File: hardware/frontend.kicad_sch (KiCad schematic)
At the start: 92 parts, among them IC201 FMMT458TA, J201 Conn_01x02, J202 Conn_01x02, J203 Conn_01x02, J204 Conn_01x02, J205 Conn_01x02, Q201 2N7002, U201 BQ769x2

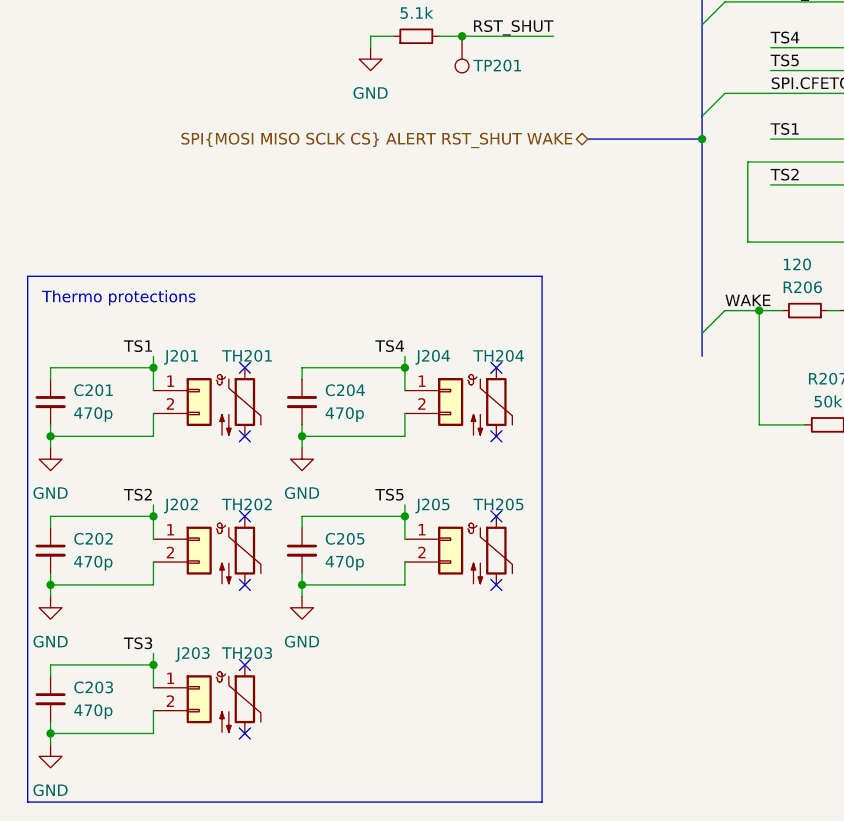
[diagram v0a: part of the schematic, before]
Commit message: change add thermoprotection
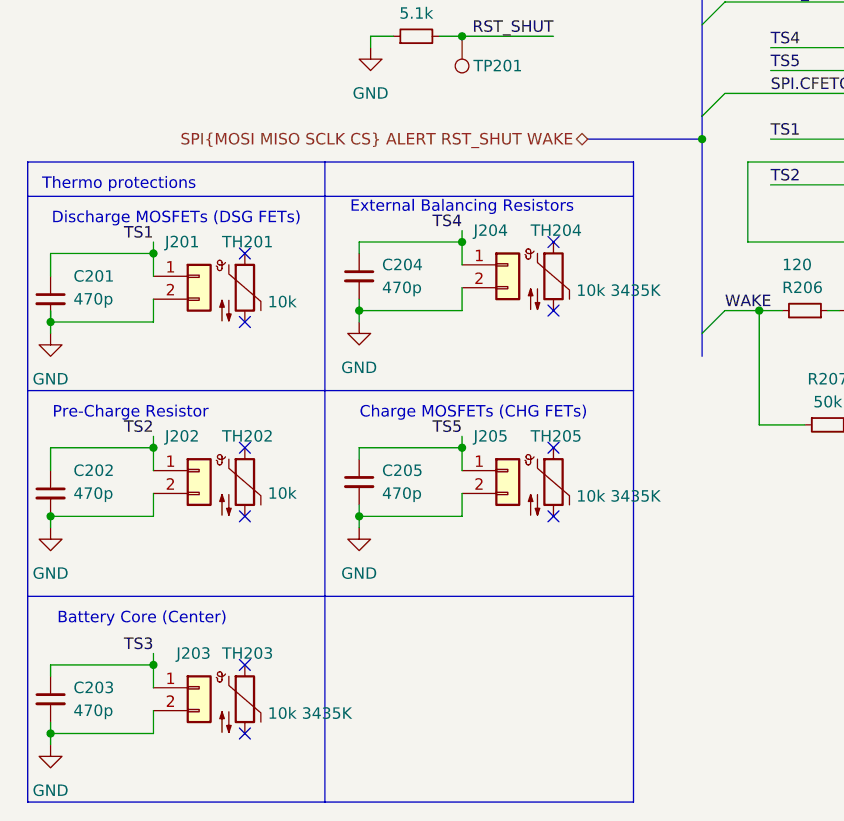
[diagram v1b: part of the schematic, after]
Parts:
- TH201, TH202: value Thermistor_NTC -> 10k; LCSC (none) -> C84036
- TH203, TH204, TH205: value Thermistor_NTC -> 10k 3435K; LCSC (none) -> C84036
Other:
- note added: "Battery Core (Center)"
- note added: "Charge MOSFETs (CHG FETs)"
- note added: "Discharge MOSFETs (DSG FETs)"
- note added: "External Balancing Resistors"
- note added: "Pre-Charge Resistor"
- moved on the sheet: C201, C202, C204, C205, J201, J202, J204, J205, TH201, TH202, TH204, TH205

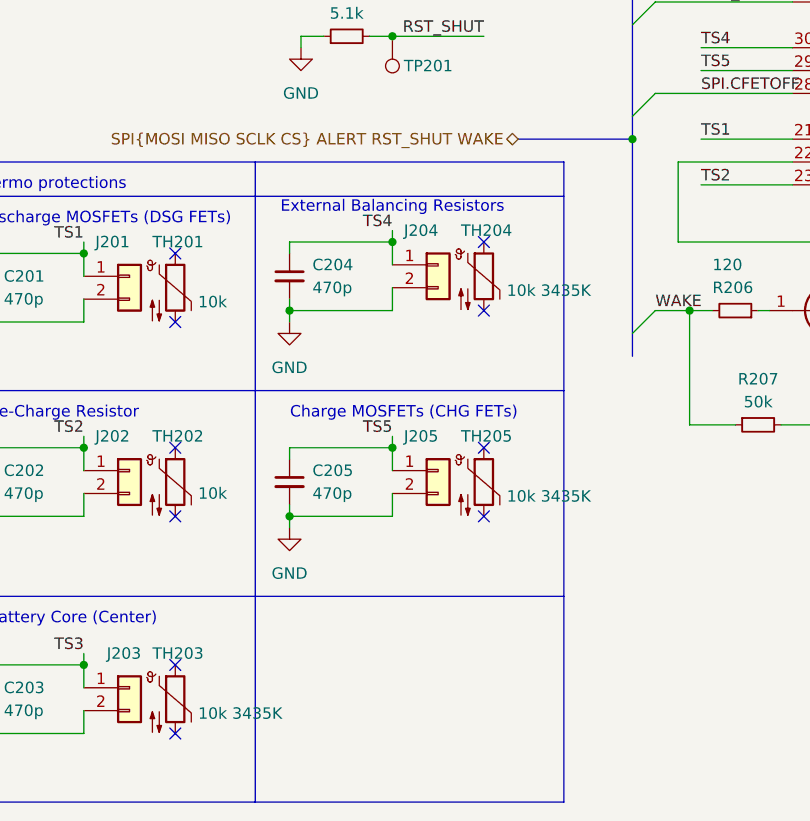
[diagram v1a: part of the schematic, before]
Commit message: change add thermoprotection
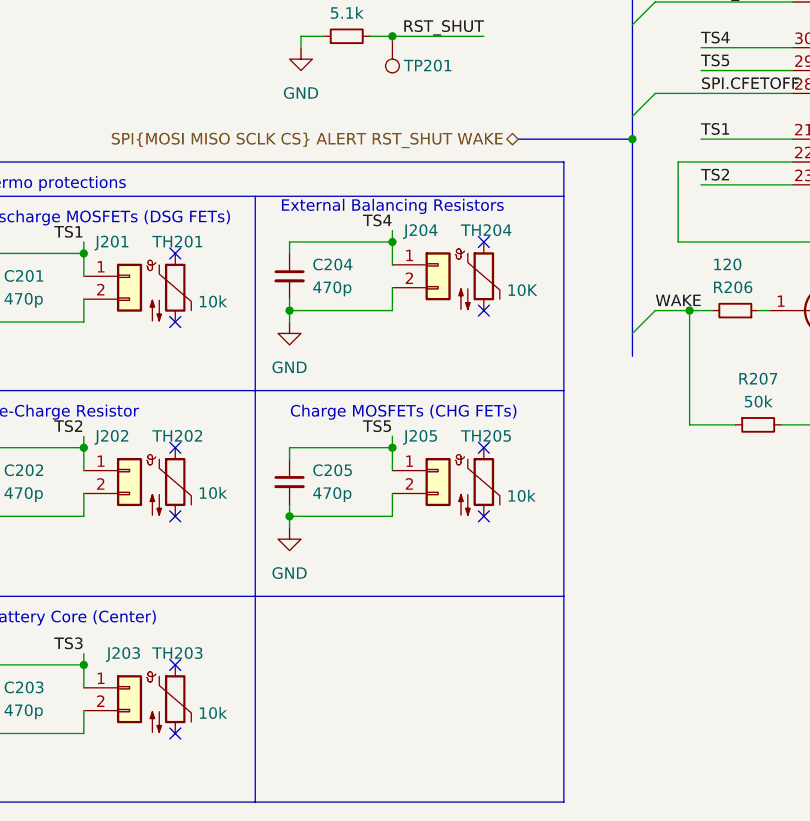
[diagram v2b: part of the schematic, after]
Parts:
- TH203, TH205: value 10k 3435K -> 10k
- TH204: value 10k 3435K -> 10K
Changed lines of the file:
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@@
 	(polyline
 		(pts
-			(xy 46.99 125.73) (xy 46.99 196.85)
+			(xy 46.99 129.54) (xy 46.99 196.85)
 		)
 		(stroke
@@
 			)
 		)
-		(property "Value" "10k 3435K"
+		(property "Value" "10K"
 			(at 74.93 140.0174 0)
 			(show_name no)
@@
 			)
 		)
-		(property "Value" "10k 3435K"
+		(property "Value" "10k"
 			(at 40.64 187.0074 0)
 			(show_name no)
@@
 			)
 		)
-		(property "Value" "10k 3435K"
+		(property "Value" "10k"
 			(at 74.93 162.8774 0)
 			(show_name no)

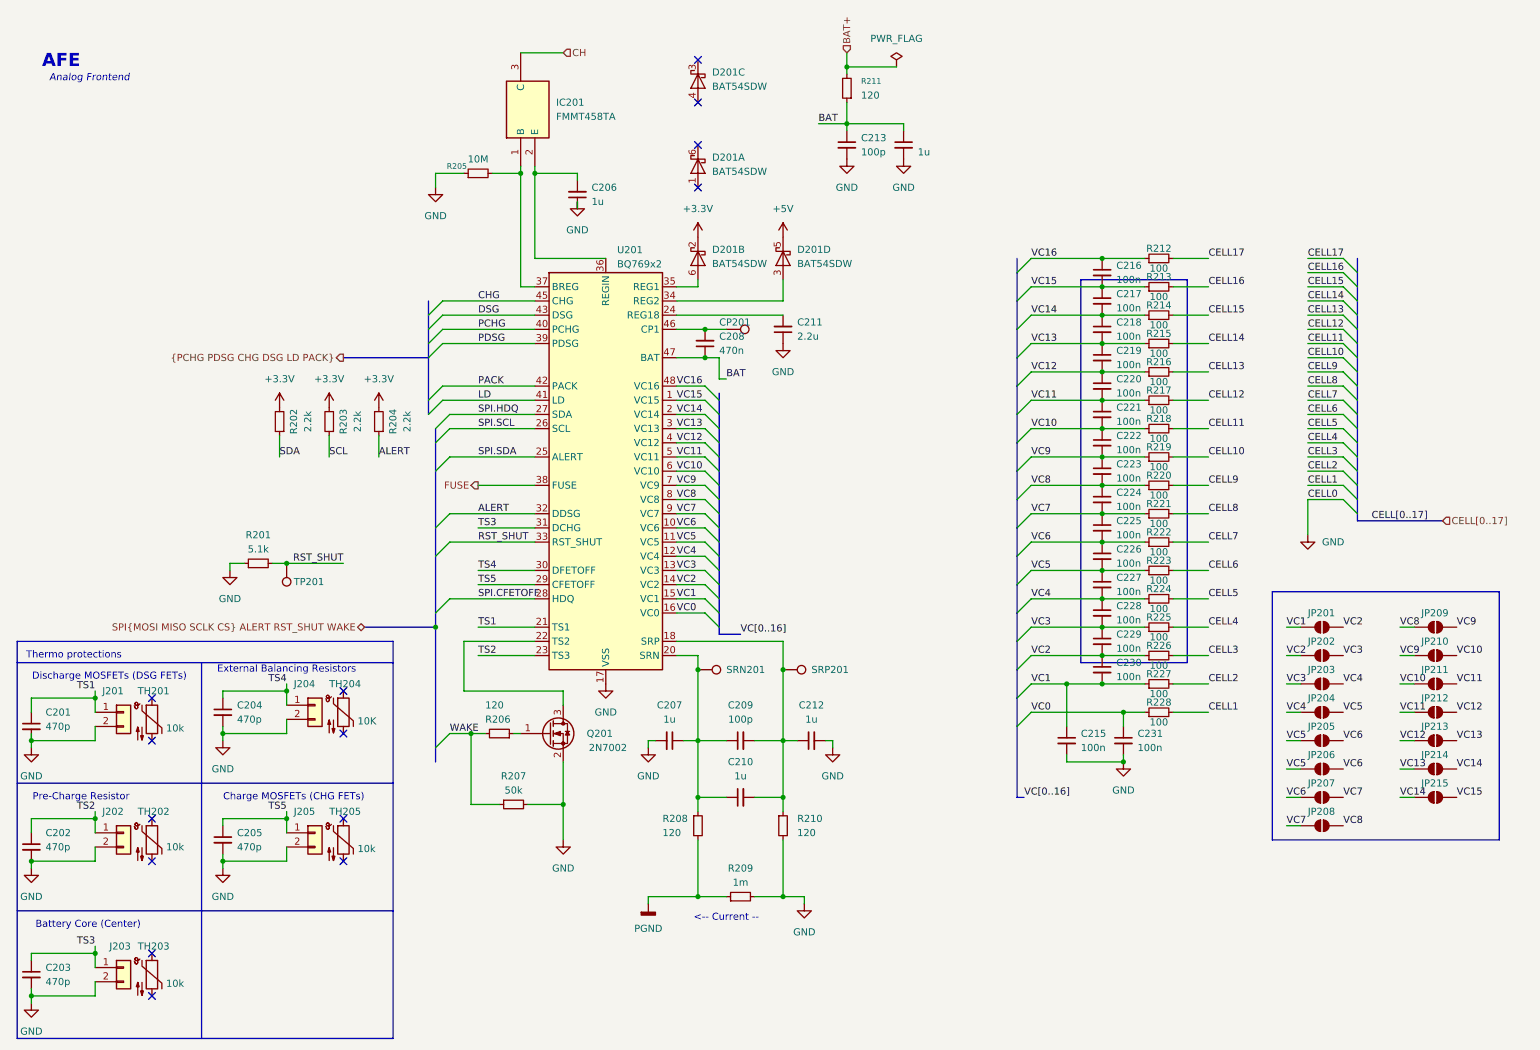
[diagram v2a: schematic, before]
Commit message: change change n transistor symbol
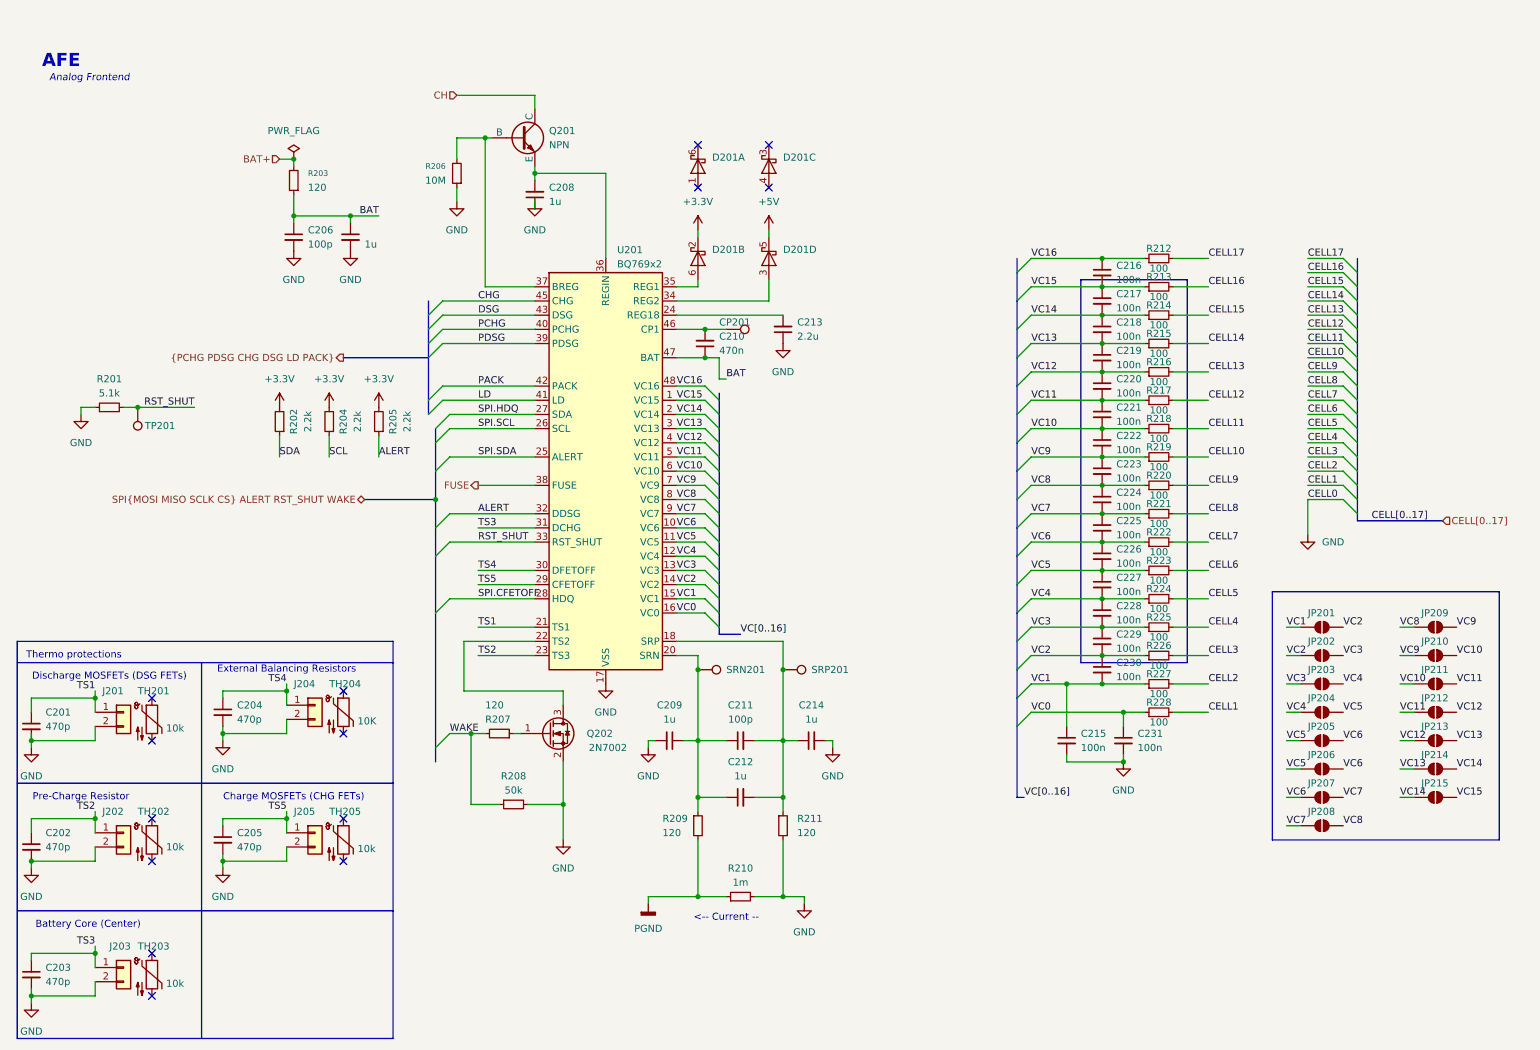
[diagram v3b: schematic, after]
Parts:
- removed IC201: FMMT458TA, Samacsys:SOT96P240X110-3N, symbol Samacsys:FMMT458TA
- added Q201: NPN, Samacsys:SOT96P240X110-3N, symbol Simulation_SPICE:NPN
- renumbered C213 to C206, C214 to C207, C206 to C208, C207 to C209, C208 to C210, C209 to C211, C210 to C212, C211 to C213, C212 to C214, Q201 to Q202, R211 to R203, R203 to R204, R204 to R205, R205 to R206, R206 to R207, R207 to R208, R208 to R209, R209 to R210, R210 to R211
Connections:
- net CH: now also Q201.1 (C)
- net at R206.2, U201.37 (BREG): now also Q201.2 (B)
- net at C208.2, U201.36 (REGIN): now also Q201.3 (E)
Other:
- moved on the sheet: C206, C208, D201C, D201D, R201, R203, R206, TP201

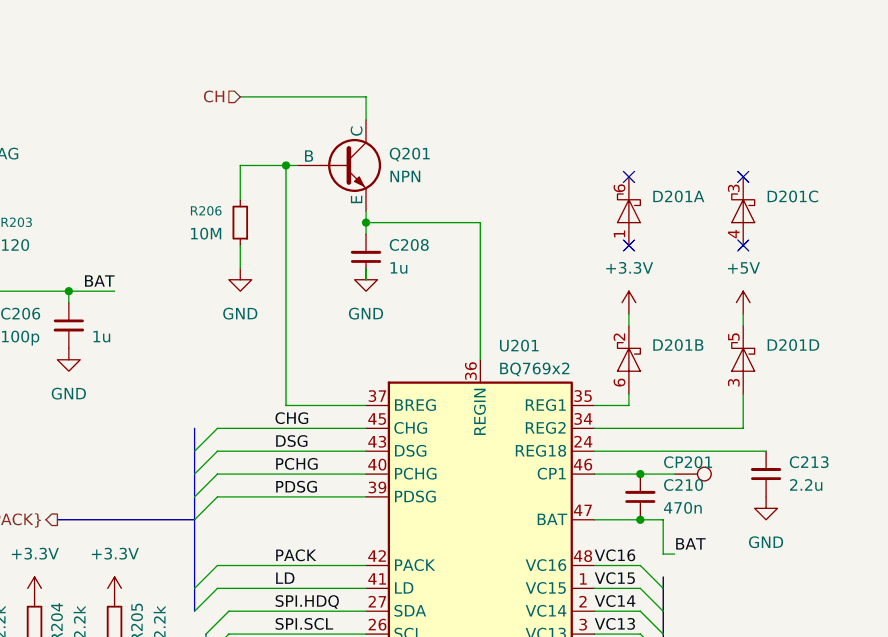
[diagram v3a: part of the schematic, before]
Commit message: hide symbols
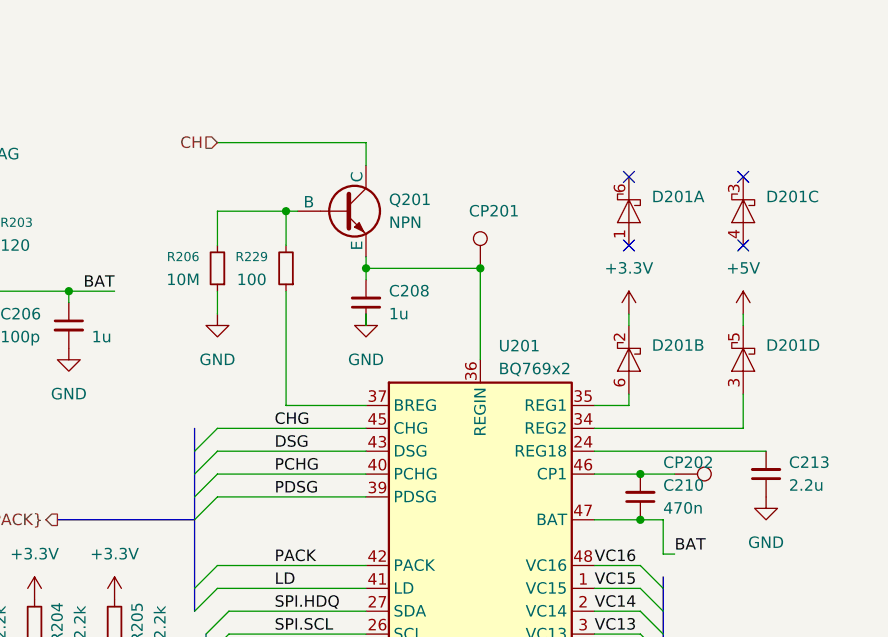
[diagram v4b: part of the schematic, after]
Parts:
- added CP201: TestPoint, TestPoint:TestPoint_Pad_D1.0mm, symbol Connector:TestPoint
- added R229: 100, Resistor_SMD:R_0805_2012Metric, symbol Device:R_Small
- renumbered CP201 to CP202
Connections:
- net at Q201.2 (B), R206.2: now also R229.2; no longer U201.37 (BREG)
- net at C208.2, Q201.3 (E), U201.36 (REGIN): now also CP201.1
- new net: R229.1, U201.37 (BREG)
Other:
- moved on the sheet: C208, Q201, R206

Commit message: fix SPI pins
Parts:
- added D202: SS110, Diode_SMD:D_SMA, symbol Device:D
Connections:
- net SPI.SDA is gone; now on net ALERT: U201.25 (ALERT)
- net ALERT: no longer U201.32 (DDSG)
- net CELL17: now also D202.2 (A)
- net TS5: now also U201.32 (DDSG); no longer U201.29 (CFETOFF)
- net CH: no longer names the net of Q201.1 (C)
- net CH: now also D202.1 (K)
- net SPI.CFETOFF renamed SPI.MOSI
- net SPI.HDQ renamed SPI.MISO
- net SPI.SCL renamed SPI.SCLK
- new net SPI.CS: U201.29 (CFETOFF)
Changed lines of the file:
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@@
 	)
 	(bus_entry
+		(at 88.9 118.11)
+		(size 2.54 -2.54)
+		(stroke
+			(width 0)
+			(type default)
+		)
+	)
+	(bus_entry
 		(at 91.44 142.24)
 		(size -2.54 2.54)
@@
 	)
 	(bus_entry
-		(at 88.9 105.41)
-		(size 2.54 -2.54)
-		(stroke
-			(width 0)
-			(type default)
-		)
-	)
-	(bus_entry
 		(at 251.46 77.47)
 		(size 2.54 2.54)
@@
 	(wire
 		(pts
-			(xy 91.44 102.87) (xy 106.68 102.87)
-		)
-		(stroke
-			(width 0)
-			(type default)
-		)
-	)
-	(wire
-		(pts
 			(xy 220.98 77.47) (xy 227.33 77.47)
 		)
@@
 	(wire
 		(pts
+			(xy 90.17 33.02) (xy 96.52 33.02)
+		)
+		(stroke
+			(width 0)
+			(type default)
+		)
+	)
+	(wire
+		(pts
 			(xy 261.62 153.67) (xy 264.16 153.67)
 		)
@@
 	(wire
 		(pts
+			(xy 91.44 115.57) (xy 106.68 115.57)
+		)
+		(stroke
+			(width 0)
+			(type default)
+		)
+	)
+	(wire
+		(pts
 			(xy 151.13 153.67) (xy 151.13 156.21)
 		)
@@
 	(wire
 		(pts
+			(xy 96.52 102.87) (xy 106.68 102.87)
+		)
+		(stroke
+			(width 0)
+			(type default)
+		)
+	)
+	(wire
+		(pts
 			(xy 111.76 147.32) (xy 111.76 154.94)
 		)
@@
 		)
 	)
-	(wire
-		(pts
-			(xy 96.52 115.57) (xy 106.68 115.57)
-		)
-		(stroke
-			(width 0)
-			(type default)
-		)
-	)
 	(bus
 		(pts
@@
 	(wire
 		(pts
+			(xy 104.14 33.02) (xy 106.68 33.02)
+		)
+		(stroke
+			(width 0)
+			(type default)
+		)
+	)
+	(wire
+		(pts
 			(xy 132.08 95.25) (xy 137.16 95.25)
 		)
@@
 	(wire
 		(pts
-			(xy 106.68 33.02) (xy 90.17 33.02)
-		)
-		(stroke
-			(width 0)
-			(type default)
-		)
-	)
-	(wire
-		(pts
 			(xy 195.58 77.47) (xy 208.28 77.47)
 		)
@@
 		)
 	)
-	(label "SPI.HDQ"
+	(label "SPI.MISO"
 		(at 96.52 85.09 0)
 		(effects
@@
 		)
 	)
-	(label "TS5"
-		(at 96.52 115.57 0)
-		(effects
-			(font
-				(size 1.27 1.27)
-			)
-			(justify left bottom)
-		)
-	)
-	(label "SPI.CFETOFF"
+	(label "SPI.MOSI"
 		(at 96.52 118.11 0)
 		(effects
@@
 		)
 	)
-	(label "SPI.SDA"
-		(at 96.52 92.71 0)
-		(effects
-			(font
-				(size 1.27 1.27)
-			)
-			(justify left bottom)
-		)
-	)
 	(label "VC6"
 		(at 251.46 148.59 0)
@@
 		)
 	)
+	(label "CELL17"
+		(at 90.17 33.02 0)
+		(effects
+			(font
+				(size 1.27 1.27)
+			)
+			(justify left bottom)
+		)
+	)
 	(label "CELL15"
 		(at 245.11 62.23 0)
@@
 		)
 	)
-	(label "ALERT"
+	(label "TS5"
 		(at 96.52 102.87 0)
 		(effects
@@
 		)
 	)
-	(label "SPI.SCL"
+	(label "SPI.SCLK"
 		(at 96.52 87.63 0)
 		(effects
@@
 		)
 	)
+	(label "SPI.CS"
+		(at 96.52 115.57 0)
+		(effects
+			(font
+				(size 1.27 1.27)
+			)
+			(justify left bottom)
+		)
+	)
 	(label "VC9"
 		(at 261.62 128.27 0)
@@
 		)
 	)
+	(label "ALERT"
+		(at 96.52 92.71 0)
+		(effects
+			(font
+				(size 1.27 1.27)
+			)
+			(justify left bottom)
+		)
+	)
 	(label "VC12"
 		(at 271.78 138.43 0)
@@
 		)
 	)
-	(hierarchical_label "CH"
-		(shape input)
-		(at 90.17 33.02 180)
-		(effects
-			(font
-				(size 1.27 1.27)
-			)
-			(justify right)
-		)
-	)
 	(hierarchical_label "FUSE"
 		(shape output)
@@
 					(unit 1)
 				)
+			)
+		)
+	)
+	(symbol
+		(lib_id "Device:D")
+		(at 100.33 33.02 180)
+		(unit 1)
+		(body_style 1)
+		(exclude_from_sim no)
+		(in_bom yes)
+		(on_board yes)
+		(in_pos_files yes)
+		(dnp no)
+		(fields_autoplaced yes)
+		(property "Reference" "D202"
+			(at 100.33 26.67 0)
+			(show_name no)
+			(do_not_autoplace no)
+			(effects
+				(font
+					(size 1.27 1.27)
+				)
+			)
+		)
+		(property "Value" "SS110"
+			(at 100.33 29.21 0)
+			(show_name no)
+			(do_not_autoplace no)
+			(effects
+				(font
+					(size 1.27 1.27)
+				)
+			)
+		)
+		(property "Footprint" "Diode_SMD:D_SMA"
+			(at 100.33 33.02 0)
+			(hide yes)
+			(show_name no)
+			(do_not_autoplace no)
+			(effects
+				(font
+					(size 1.27 1.27)
+				)
+			)
+		)
+		(property "Datasheet" ""
+			(at 100.33 33.02 0)
+			(hide yes)
+			(show_name no)
+			(do_not_autoplace no)
+			(effects
+				(font
+					(size 1.27 1.27)
+				)
+			)
+		)
+		(property "Description" "Diode"
+			(at 100.33 33.02 0)
+			(hide yes)
+			(show_name no)
+			(do_not_autoplace no)
+			(effects
+				(font
+					(size 1.27 1.27)
+				)
+			)
+		)
+		(property "Sim.Device" "D"
+			(at 100.33 33.02 0)
+			(hide yes)
+			(show_name no)
+			(do_not_autoplace no)
+			(effects
+				(font
+					(size 1.27 1.27)
+				)
+			)
+		)
+		(property "Sim.Pins" "1=K 2=A"
+			(at 100.33 33.02 0)
+			(hide yes)
+			(show_name no)
+			(do_not_autoplace no)
+			(effects
+				(font
+					(size 1.27 1.27)
+				)
+			)
+		)
+		(property "LCSC" "C18199178"
+			(at 100.33 26.67 0)
+			(hide yes)
+			(show_name no)
+			(do_not_autoplace no)
+			(effects
+				(font
+					(size 1.27 1.27)
+				)
+			)
+		)
+		(pin "1"
+		)
+		(pin "2"
+		)
+		(instances
+			(project "wafel-eval-board"
+				(path "/3e668e3e-3e16-4665-a807-4735962c41d3/204526d9-bdaf-4b36-9252-b50630c4791c"
+					(reference "D202")
+					(unit 1)
+				)
